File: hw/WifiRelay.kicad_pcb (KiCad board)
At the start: 2 copper layers, 94 x 54 mm, 34 parts, among them J1 CONN_01X02, J2 CONN_01X06, J3 CONN_01X02, J4 CONN_01X02, J5 TEST_1P, K1 Songle-SRD-05VDC-SL-C, K2 Songle-SRD-05VDC-SL-C, Q1 MMSS8050-H, Q2 MMSS8050-H, SW1 SW_Push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

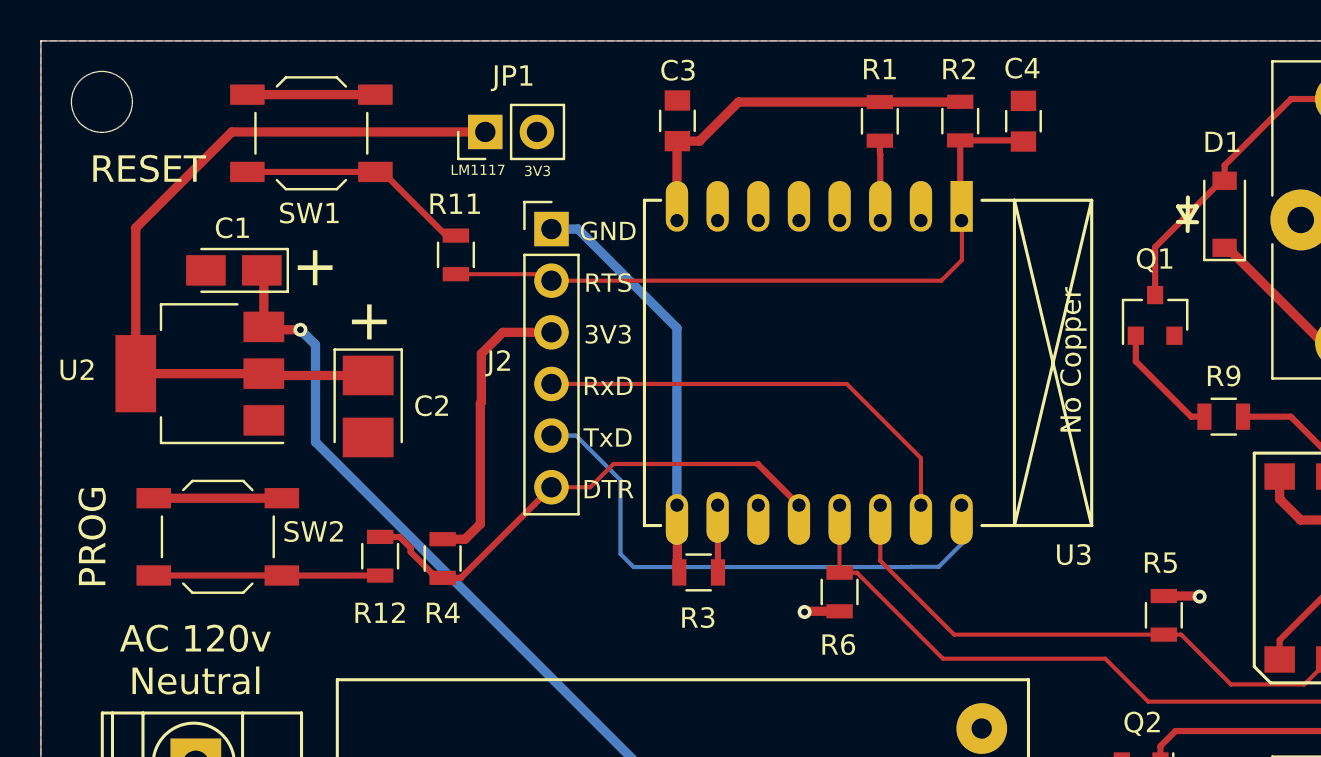
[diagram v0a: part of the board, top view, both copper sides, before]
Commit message: Silkscreen updates to programming header, changed 3.3v power jumper to two positions
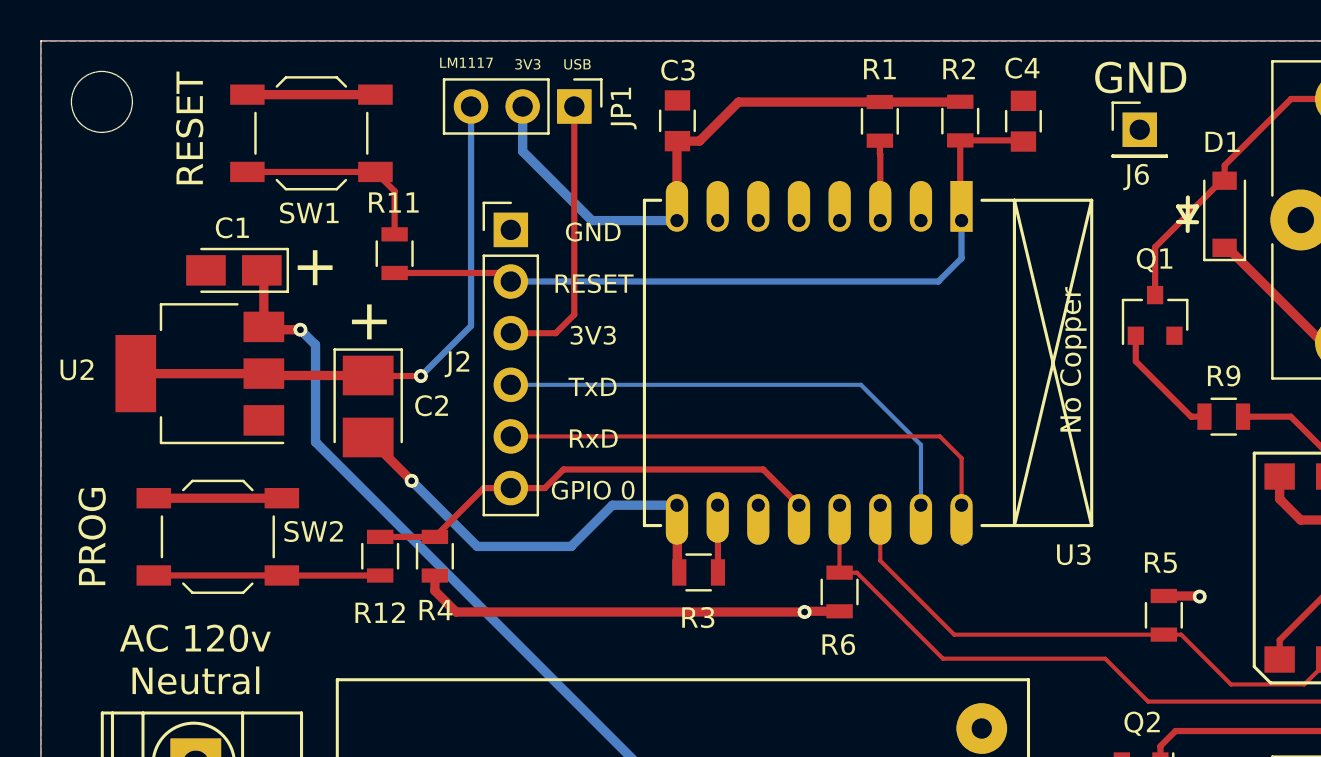
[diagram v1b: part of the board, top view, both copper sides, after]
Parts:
- added J6: TEST_1P, Pin_Headers:Pin_Header_Straight_1x01_Pitch2.54mm, F.Cu at (112.1, 80.1)
- JP1: value Jumper -> Jumper_Dual; footprint Pin_Headers:Pin_Header_Straight_1x02_Pitch2.54mm -> Pin_Headers:Pin_Header_Straight_1x03_Pitch2.54mm
- moved JP1 4.55 mm to (84.3, 78.9), turned to 270 degrees
- moved R11 3.02 mm to (75.4, 86.2)
- moved J2 2.00 mm to (81.2, 85.0)
- moved R4 0.40 mm to (77.4, 101.1), turned to 90 degrees
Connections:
- C2 pad 1: Net-(C2-Pad1) -> /3V3REG
- J2 pad 3: +3V3 -> Net-(J2-Pad3)
- JP1 pad 1: Net-(C2-Pad1) -> Net-(J2-Pad3)
- U2 pad 2: Net-(C2-Pad1) -> /3V3REG
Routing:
- net Net-(C2-Pad1): track 38.4 -> 0.00 mm
- net /3V3REG: track 0.00 -> 28.9 mm, vias 0 -> 1
- net +3V3: track 41.2 -> 57.6 mm
- net Net-(J2-Pad3): track 0.00 -> 13.7 mm
- net /RESET: track 34.9 -> 37.9 mm
- net /GPIO0: track 25.4 -> 22.7 mm
- net /RXD: track 22.0 -> 24.4 mm
- net Net-(R11-Pad2): track 11.6 -> 10.1 mm
- net GND: track 34.0 -> 35.2 mm, vias 0 -> 1
- net /TXD: track 27.5 -> 27.0 mm
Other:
- board text added: "GPIO 0"
- board text added: "USB"
- board text added: "WiFi Controller v1.1 Rev A Jeff Davis, N0DY 6/17/2017"
- board text removed: "DTR"
- board text removed: "RTS"
- board text removed: "WiFi Controller, v1.1 Jeff Davis, N0DY 5/28/2017"

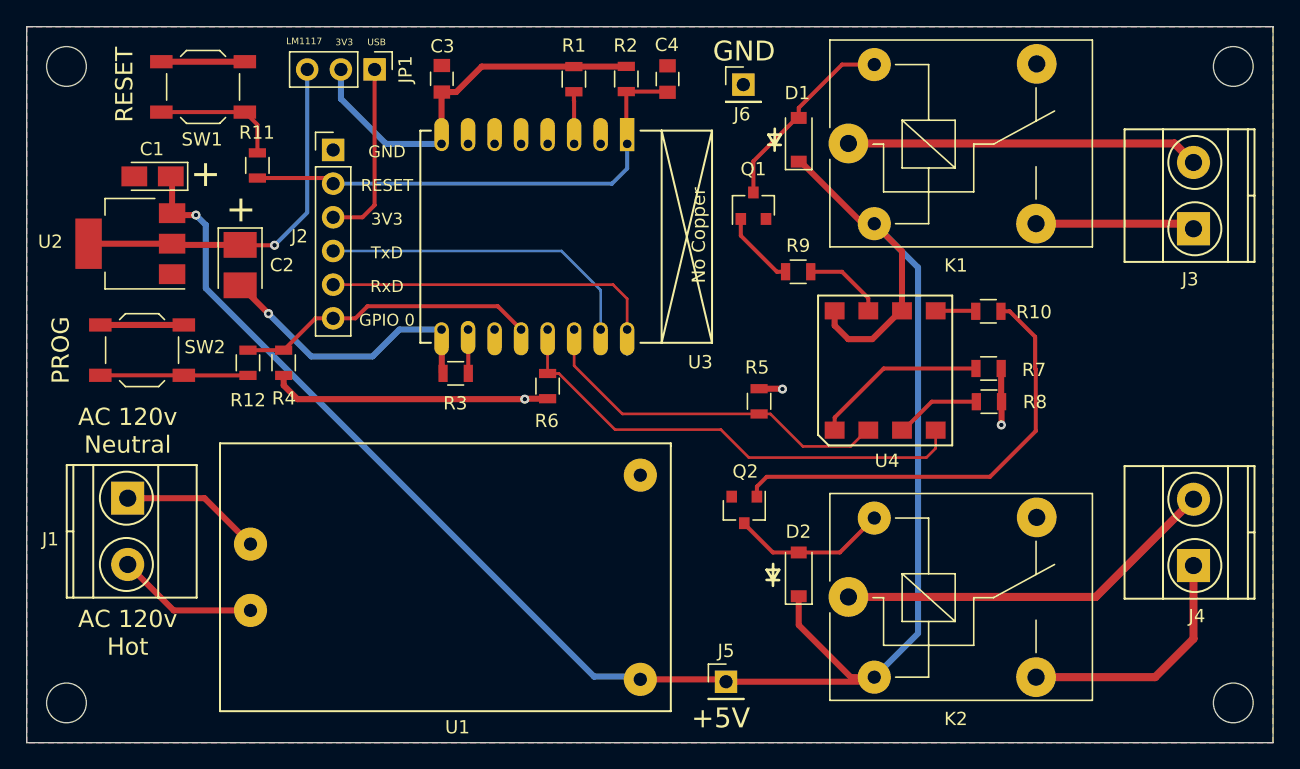
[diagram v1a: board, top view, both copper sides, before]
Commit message: Updated symbol and footprint libraries to use KiCad 5 versions.
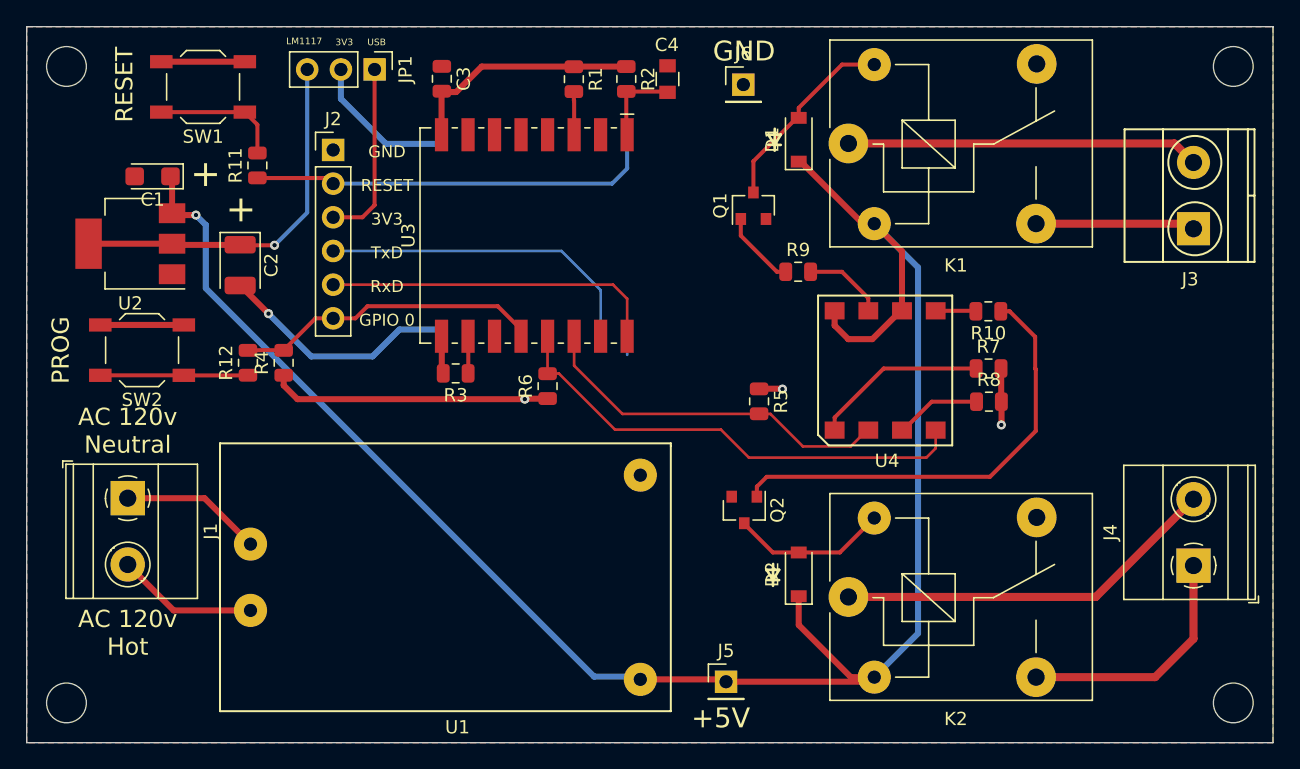
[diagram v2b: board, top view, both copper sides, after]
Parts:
- C1: footprint Capacitors_Tantalum_SMD:CP_Tantalum_Case-A_EIA-3216-18_Reflow -> Capacitor_Tantalum_SMD:CP_EIA-3216-18_Kemet-A
- C2: footprint Capacitors_Tantalum_SMD:CP_Tantalum_Case-B_EIA-3528-21_Reflow -> Capacitor_Tantalum_SMD:CP_EIA-3528-21_Kemet-B
- C3: footprint Capacitors_SMD:C_0805 -> Capacitor_SMD:C_0805_2012Metric
- D1, D2: footprint Diodes_SMD:D_SOD-123 -> Diode_SMD:D_SOD-123
- J1, J4: footprint Connectors_Terminal_Blocks:TerminalBlock_Pheonix_MKDS1.5-2pol -> TerminalBlock_Phoenix:TerminalBlock_Phoenix_MKDS-1,5-2_1x02_P5.00mm_Horizontal
- J2: footprint Pin_Headers:Pin_Header_Straight_1x06_Pitch2.54mm -> Connector_PinHeader_2.54mm:PinHeader_1x06_P2.54mm_Vertical
- J5, J6: footprint Pin_Headers:Pin_Header_Straight_1x01_Pitch2.54mm -> Connector_PinHeader_2.54mm:PinHeader_1x01_P2.54mm_Vertical
- JP1: footprint Pin_Headers:Pin_Header_Straight_1x03_Pitch2.54mm -> Connector_PinHeader_2.54mm:PinHeader_1x03_P2.54mm_Vertical
- K1, K2: footprint Relays_THT:Relay_SPDT_SANYOU_SRD_Series_Form_C -> Relay_THT:Relay_SPDT_SANYOU_SRD_Series_Form_C
- Q1, Q2: footprint TO_SOT_Packages_SMD:SOT-23 -> Package_TO_SOT_SMD:SOT-23
- R1, R10, R11, R12, R2, R3, R4, R5, R6, R7, R8, R9: footprint Resistors_SMD:R_0805 -> Resistor_SMD:R_0805_2012Metric
- SW1, SW2: footprint Buttons_Switches_SMD:SW_SPST_TL3342 -> Button_Switch_SMD:SW_SPST_TL3342
- U2: footprint TO_SOT_Packages_SMD:SOT-223-3Lead_TabPin2 -> Package_TO_SOT_SMD:SOT-223-3_TabPin2
- U3: value ESP-07v2 -> ESP-07; footprint ESP8266:ESP-07v2 -> RF_Module:ESP-07
- moved U3 8.47 mm to (98.4, 91.5)
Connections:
- K1 pad 4: (no net) -> Net-(K1-Pad4)
- K2 pad 4: (no net) -> Net-(K2-Pad4)
- U3 pad 11: (no net) -> Net-(U3-Pad11)
- U3 pad 2: (no net) -> Net-(U3-Pad2)
- U3 pad 4: (no net) -> Net-(U3-Pad4)
- U3 pad 5: (no net) -> Net-(U3-Pad5)
- U3 pad 6: (no net) -> Net-(U3-Pad6)
- U3 pad 7: (no net) -> Net-(U3-Pad7)
